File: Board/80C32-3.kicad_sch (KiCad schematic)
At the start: 51 parts, among them CN2 POWER, CN4 SERIAL, J1 EPROM-SELECT, J2 RAM-SELECT, J3 EEPROM-SELECT, X1 12.000MHz

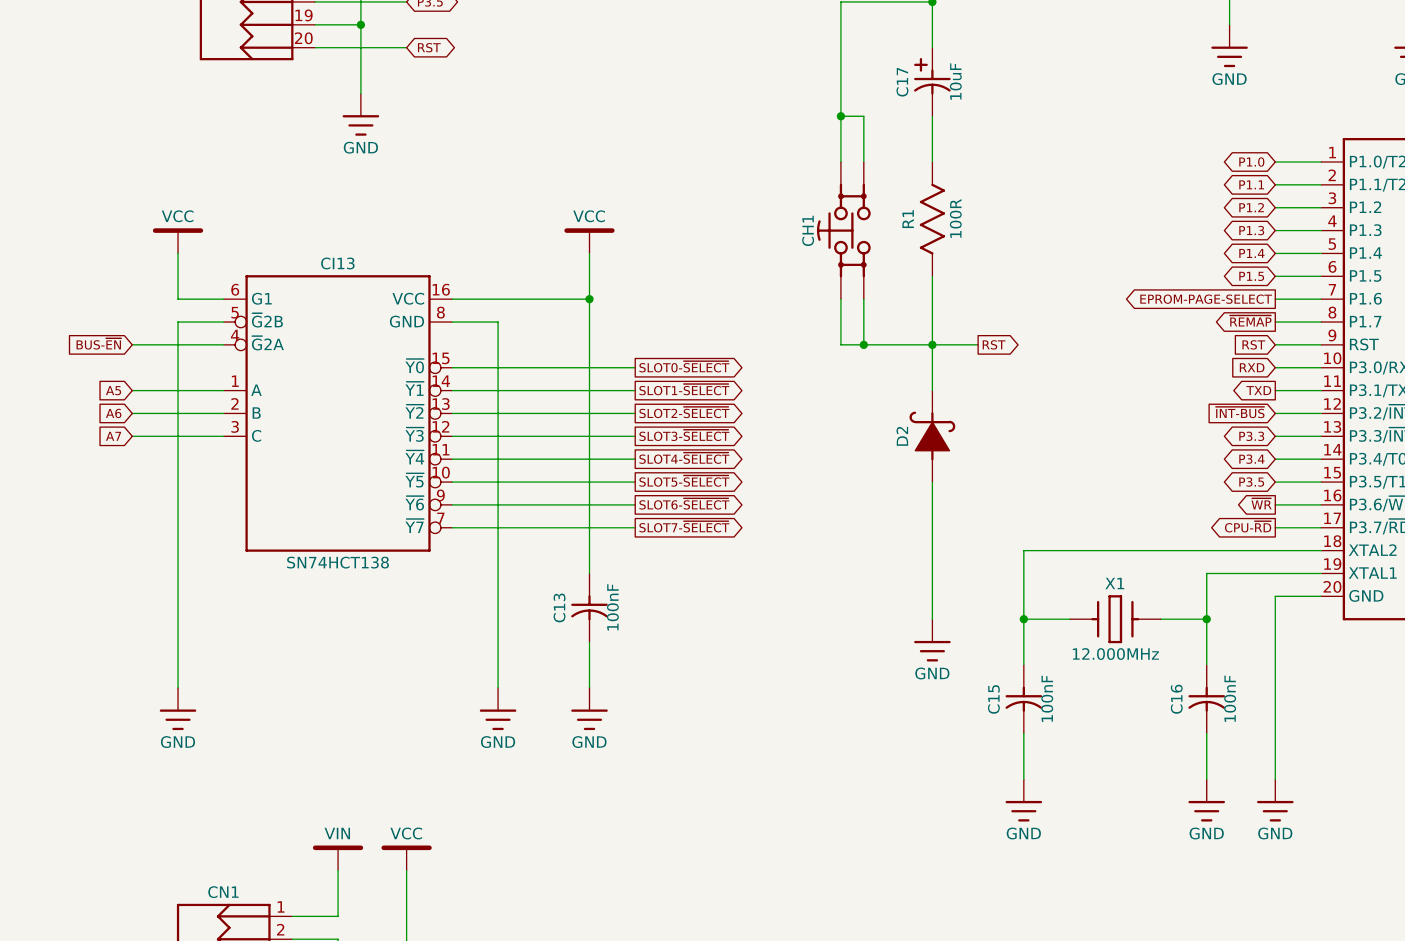
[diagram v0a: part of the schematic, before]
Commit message: - Corrected value of the crystal load capacitors. - Added note stating that CI13 is not implemented in this version of the board. - Added missing 3D model.
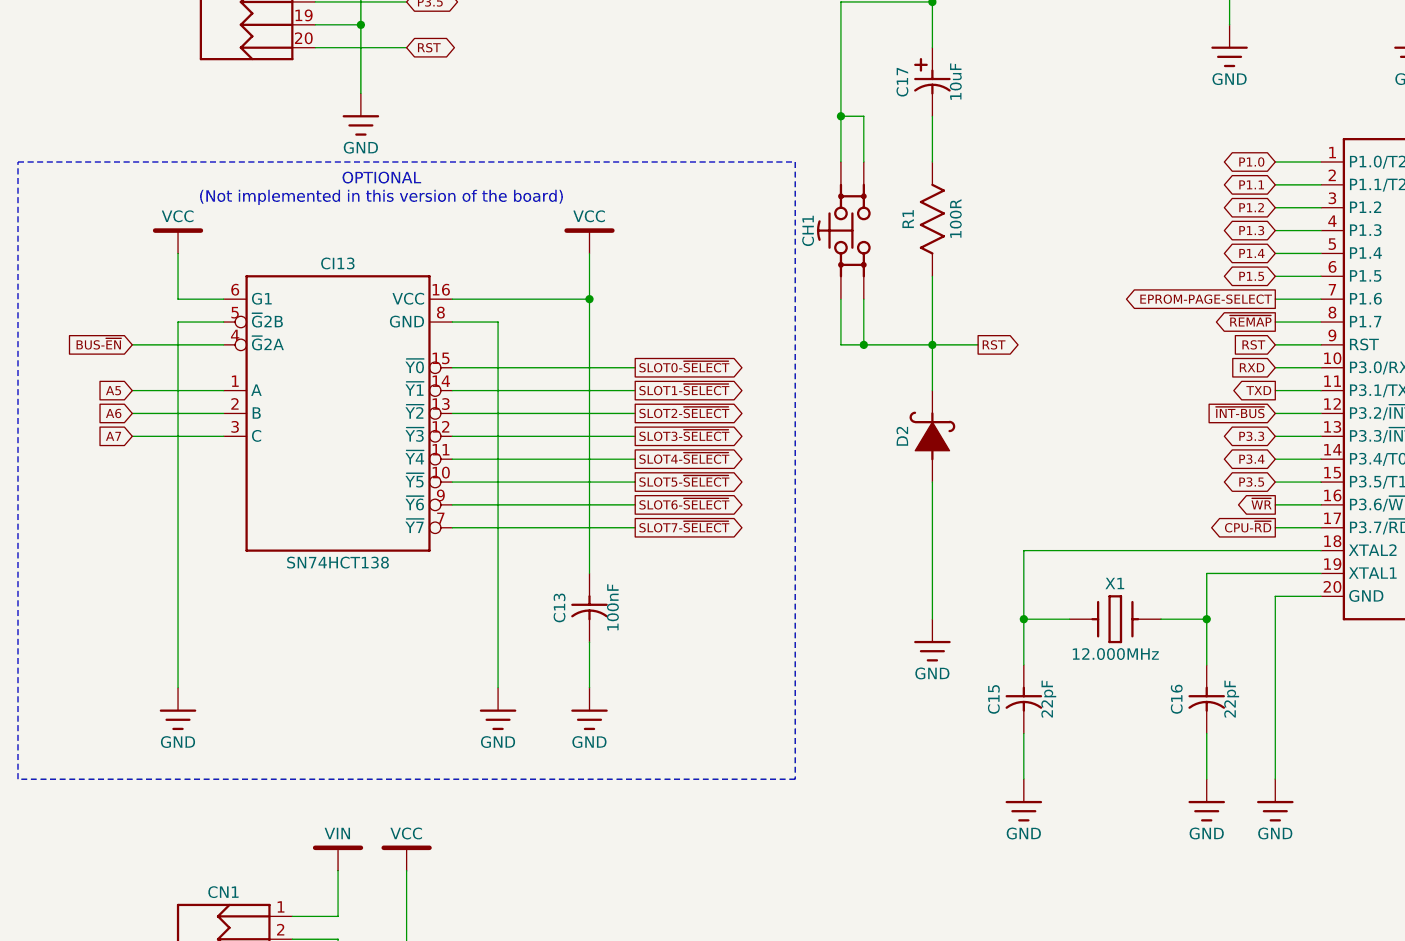
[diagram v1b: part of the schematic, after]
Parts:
- C15, C16: value 100nF -> 22pF
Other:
- note added: "OPTIONAL (Not implemented in this version of the board)"
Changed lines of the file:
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@@
 	(generator_version "9.0")
 	(paper "A2")
+	(rectangle
+		(start 22.86 149.86)
+		(end 109.22 218.44)
+		(stroke
+			(width 0)
+			(type dash)
+		)
+		(fill
+			(type none)
+		)
+	)
+	(text "OPTIONAL\n(Not implemented in this version of the board)"
+		(exclude_from_sim no)
+		(at 63.246 152.908 0)
+		(effects
+			(font
+				(size 1.27 1.27)
+			)
+		)
+	)
 	(junction
 		(at 58.42 276.86)
@@
 			)
 		)
-		(property "Value" "100nF"
+		(property "Value" "22pF"
 			(at 136.525 209.55 90)
 			(effects
@@
 			)
 		)
-		(property "Value" "100nF"
+		(property "Value" "22pF"
 			(at 156.845 209.55 90)
 			(effects

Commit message: Added PDF files with the schematics.
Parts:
- D2: value ~ -> 1N4148
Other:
- note added: "0"
- note added: "1"
- note added: "13"
- note added: "14"
- note added: "15"
- note added: "2026/03/10"
- note added: "3"
- note added: "4"
- note added: "5"
- note added: "6"
- note added: "7"
- note added: "9"
- note added: "A0"
- note added: "A1"
- note added: "A2"
- note added: "A3"
- note added: "A4"
- note added: "A5"
- note added: "A6"
- note added: "A7"
- note added: "By Isaac Marino Bavaresco"
- note added: "CI3 (EPROM) J1: 2732: 13-14 2764: 1-4, 3-6 27128: 1-4, 3-6 27256: 1-4, 5-6 27512: 4-7, 5-6"
- note added: "CI4 (RAM) J2: All: 6-9 (enable ~{WR}) 6264: 6-9, 13-14 (CE2 enabled) 62128: 6-9, 62256: 4-5, 6-9, 14-15"
- note added: "CI5 (EEPROM) J3: All: 6-9 (enable ~{WR}), 3-6 (Write protect) All: 14-15 28C64: 28C256: 4-5"
- note added: "D0"
- note added: "D1"
- note added: "D2"
- note added: "D3"
- note added: "D4"
- note added: "D5"
- note added: "D6"
- note added: "D7"
- note added: "GND"
- note added: "JUMPERS CONFIGURATION"
- note added: "N.C."
- note added: "P1.2"
- note added: "P1.3"
- note added: "P1.4"
- note added: "P1.5"
- note added: "RST"
- note added: "RXD/P3.0"
- note added: "RXD/P3.1"
- note added: "Retro-Computing Didactic 80C32 Board"
- note added: "T0/P3.4"
- note added: "T1/P3.5"
- note added: "T2/P1.0"
- note added: "T2EX/P1.1"
- note added: "VCC"
- note added: "Vin"
- note added: "~{INT0}"
- note added: "~{INT0}/P3.2"
- note added: "~{INT1}/P3.3"
- note added: "~{RD}"
- note added: "~{WR}"
